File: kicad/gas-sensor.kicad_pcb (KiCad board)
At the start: 2 copper layers, 25 parts, among them J1 RJ12, U1 DS18B20, U2 FT232RL, U3 MCP1703A-3302_SOT23, U4 ATmega328P-AU, Y1 8MHz

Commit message: minor changes
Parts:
- added U5: DHT22, gas_sensor:DHT22, F.Cu at (60.9, 54.8)
- moved C3 96.5 mm to (76.9, 80.2), turned to 180 degrees
- moved C4 96.5 mm to (78.0, 85.4), turned to 180 degrees
- moved R2 83.9 mm to (84.5, 85.5)
- moved R1 63.9 mm to (105.1, 79.3), turned to 180 degrees
- moved R3 61.5 mm to (126.0, 72.2), turned to 180 degrees
- moved R4 53.8 mm to (143.1, 72.9), turned to 180 degrees
- moved C2 52.8 mm to (105.1, 82.8), turned to 180 degrees
- moved C6 33.7 mm to (125.8, 108.5)
- moved C5 33.6 mm to (125.3, 103.6), turned to 180 degrees
- moved C7 31.2 mm to (125.8, 110.8)
- moved U4 12.9 mm to (97.3, 97.8)
- moved D3 9.96 mm to (132.9, 105.8)
- moved U2 9.29 mm to (118.0, 93.2)
- moved D1 7.46 mm to (132.8, 96.4)
- moved U3 6.54 mm to (120.7, 106.4)
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
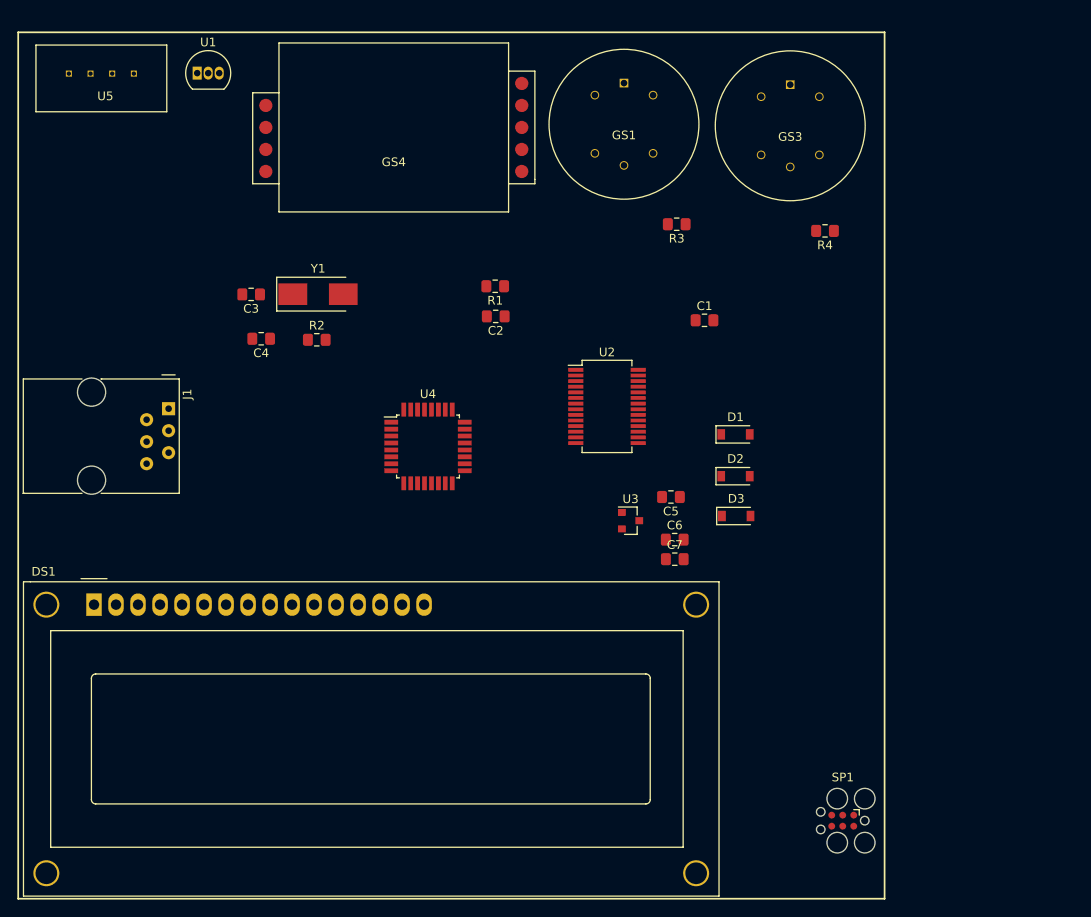
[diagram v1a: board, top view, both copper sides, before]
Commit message: First version of PCB
with 3D components
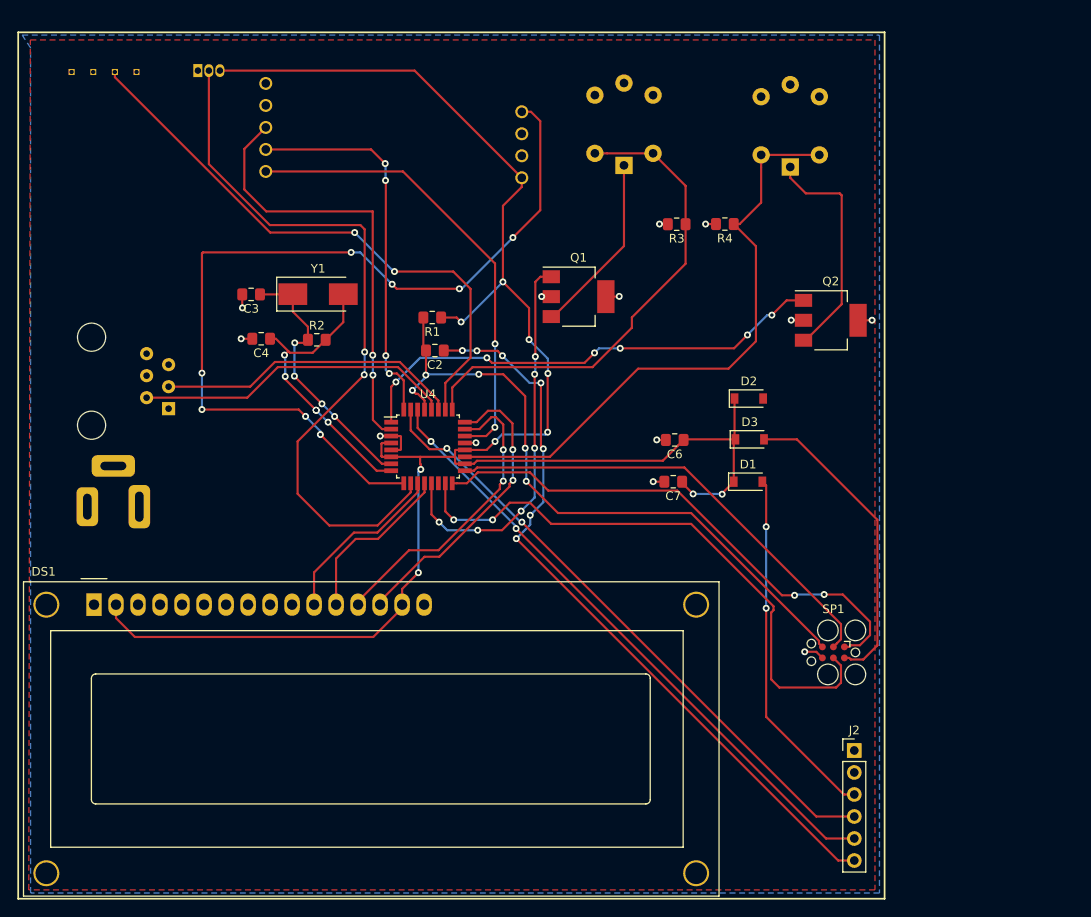
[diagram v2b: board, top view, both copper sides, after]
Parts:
- removed C1: 100nF, Capacitor_SMD:C_0805_2012Metric_Pad1.15x1.40mm_HandSolder
- removed C5: 10u, Capacitor_SMD:C_0805_2012Metric_Pad1.15x1.40mm_HandSolder
- removed U2: FT232RL, Package_SO:SSOP-28_5.3x10.2mm_P0.65mm
- removed U3: MCP1703A-3302_SOT23, Package_TO_SOT_SMD:SOT-23
- added J2: Conn FT232RL, Connector_PinHeader_2.54mm:PinHeader_1x06_P2.54mm_Vertical, F.Cu at (146.5, 132.9)
- added J3: PJ-017DH, gas_sensor:PC-017C, B.Cu at (58.0, 104.8)
- added Q1: BSP75, Package_TO_SOT_SMD:SOT-223-3_TabPin2, F.Cu at (114.7, 80.5)
- added Q2: BSP75, Package_TO_SOT_SMD:SOT-223-3_TabPin2, F.Cu at (143.8, 83.2)
- GS1, GS3, GS4, J1, U1, U5: moved to B.Cu
- moved SP1 19.5 mm to (144.1, 121.6)
- moved R4 11.6 mm to (131.6, 72.1)
- moved C6 11.5 mm to (125.8, 97.0), turned to 180 degrees
- moved D2 9.09 mm to (134.3, 92.3)
- moved D3 8.99 mm to (134.4, 97.0)
- moved C7 8.94 mm to (125.6, 101.9), turned to 180 degrees
- moved R1 8.11 mm to (97.8, 82.9)
- moved C2 8.05 mm to (98.1, 86.7)
- moved D1 5.65 mm to (134.2, 101.9)
- moved U5 2.20 mm to (58.7, 54.6), turned to 180 degrees
- moved U1 0.30 mm to (70.7, 54.4)
- turned GS4 to 180 degrees
- turned J1 to 90 degrees
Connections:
- net +BATT renamed Net-(J1-Pad5)
- C6 pad 1: +3V3 -> VCC
- C7 pad 1: +3V3 -> VCC
- D1 pad 1: Net-(C5-Pad1) -> VCC
- D2 pad 1: Net-(C5-Pad1) -> VCC
- D3 pad 1: Net-(C5-Pad1) -> VCC
- DS1 pad 15: +5V -> VCC
- DS1 pad 2: +5V -> VCC
- GS1 pad 1: +5V -> /Sensor1
- GS1 pad 2: +5V -> /Sensor1
- GS1 pad 3: /Sensor1 -> +5V
- GS1 pad 4: /Sensor1 -> +5V
- GS1 pad 6: GND -> Net-(GS1-Pad6)
- GS3 pad 1: +5V -> /Sensor2
- GS3 pad 2: +5V -> /Sensor2
- GS3 pad 3: /Sensor3 -> +5V
- GS3 pad 4: /Sensor3 -> +5V
- GS3 pad 6: GND -> Net-(GS3-Pad6)
- GS4 pad 1: /Sensor4 -> /Sensor3
- GS4 pad 6: +5V -> VCC
- J1 pad 1: +5V -> Net-(J1-Pad1)
- R1 pad 1: +3V3 -> VCC
- R4 pad 1: /Sensor3 -> /Sensor2
- U1 pad 3: +5V -> VCC
- U4 pad 1: Net-(U4-Pad1) -> /Sensor2_ON
- U4 pad 13: Net-(U4-Pad13) -> /Sensor1_ON
- U4 pad 19: /Sensor3 -> /Sensor2
- U4 pad 20: +5V -> VCC
- U4 pad 22: /Sensor4 -> /Sensor3
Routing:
- net VCC: track 0.00 -> 211.7 mm, vias 0 -> 10
- net /PWM_MH-Z19: track 0.00 -> 102.5 mm, vias 0 -> 8
- net /DTR: track 0.00 -> 86.5 mm, vias 0 -> 7
- net /TEMP: track 0.00 -> 82.8 mm, vias 0 -> 2
- net /RESET: track 0.00 -> 77.2 mm, vias 0 -> 5
- net /RX: track 0.00 -> 72.3 mm, vias 0 -> 2
- net /TX: track 0.00 -> 72.1 mm, vias 0 -> 2
- net /Sensor2: track 0.00 -> 70.1 mm
- net /MOSI: track 0.00 -> 67.8 mm, vias 0 -> 2
- net /HUM: track 0.00 -> 66.9 mm, vias 0 -> 2
- net /MISO: track 0.00 -> 61.0 mm, vias 0 -> 2
- net /Sensor1: track 0.00 -> 57.1 mm
- net /Sensor2_ON: track 0.00 -> 56.3 mm, vias 0 -> 6
- net /SCK: track 0.00 -> 54.1 mm
- net /Sensor3: track 0.00 -> 53.7 mm, vias 0 -> 2
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- added copper zone on F.Cu, net +5V
- added copper zone on B.Cu, net GND

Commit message: update
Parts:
- added C1: 100nF, Capacitor_SMD:C_0805_2012Metric_Pad1.15x1.40mm_HandSolder, F.Cu at (89.4, 88.0)
- added J4: hole, MountingHole:MountingHole_3.2mm_M3, F.Cu at (146.6, 53.5)
- added J5: hole, MountingHole:MountingHole_3.2mm_M3, F.Cu at (53.4, 139.3)
- added J6: hole, MountingHole:MountingHole_3.2mm_M3, F.Cu at (53.6, 53.6)
- added J7: hole, MountingHole:MountingHole_3.2mm_M3, F.Cu at (146.2, 138.8)
- added R5: R, Capacitor_SMD:C_0805_2012Metric_Pad1.15x1.40mm_HandSolder, F.Cu at (102.1, 102.7)
- J3: value PJ-017DH -> 5V_Power_source; footprint gas_sensor:PC-017C -> Connector_BarrelJack:BarrelJack_Horizontal
- Y1: footprint Crystal:Crystal_SMD_0603-2Pin_6.0x3.5mm_HandSoldering -> Crystal:Crystal_SMD_5032-2Pin_5.0x3.2mm_HandSoldering
- moved J2 100.1 mm to (53.9, 94.8)
- moved J3 80.3 mm to (136.1, 86.0), turned to 180 degrees
- moved SP1 17.2 mm to (145.0, 104.4)
- moved C3 16.6 mm to (81.0, 96.3), turned to 90 degrees
- moved Y1 13.5 mm to (86.0, 93.6), turned to 90 degrees
- moved Q2 12.3 mm to (135.6, 74.1), turned to 270 degrees
- moved DS1 11.0 mm to (66.5, 108.2)
- moved U5 10.0 mm to (60.6, 64.4), turned to 0 degrees
- moved R2 9.28 mm to (89.5, 93.3), turned to 90 degrees
- moved U1 9.26 mm to (61.5, 53.7)
- moved D1 9.06 mm to (127.7, 95.5)
- moved D3 8.94 mm to (127.7, 91.1)
- moved C2 8.87 mm to (93.5, 79.1), turned to 0 degrees
- moved D2 8.81 mm to (128.0, 86.1)
- moved J1 8.73 mm to (67.8, 84.7)
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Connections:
- DS1 pad 15: VCC -> Net-(DS1-Pad15)
- DS1 pad 3: Net-(DS1-Pad3) -> VCC
- DS1 pad 4: Net-(DS1-Pad4) -> /LCD_RS
- DS1 pad 5: Net-(DS1-Pad5) -> /LCD_RW
- DS1 pad 6: Net-(DS1-Pad6) -> /LCD_E
- J3 pad 3: GND -> (no net)
- U1 pad 3: VCC -> +5V
- U4 pad 15: /MOSI -> /LCD_E
- U4 pad 16: /MISO -> /LCD_RW
- U4 pad 17: /SCK -> /LCD_RS
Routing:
- net VCC: track 211.7 -> 0.00 mm, vias 10 -> 0
- net /PWM_MH-Z19: track 102.5 -> 0.00 mm, vias 8 -> 0
- net /DTR: track 86.5 -> 0.00 mm, vias 7 -> 0
- net /TEMP: track 82.8 -> 0.00 mm, vias 2 -> 0
- net /RESET: track 77.2 -> 0.00 mm, vias 5 -> 0
- net /RX: track 72.3 -> 0.00 mm, vias 2 -> 0
- net /TX: track 72.1 -> 0.00 mm, vias 2 -> 0
- net /Sensor2: track 70.1 -> 0.00 mm
- net /MOSI: track 67.8 -> 0.00 mm, vias 2 -> 0
- net /HUM: track 66.9 -> 0.00 mm, vias 2 -> 0
- net /MISO: track 61.0 -> 0.00 mm, vias 2 -> 0
- net /Sensor1: track 57.1 -> 0.00 mm
- net /Sensor2_ON: track 56.3 -> 0.00 mm, vias 6 -> 0
- net /SCK: track 54.1 -> 0.00 mm
- net /Sensor3: track 53.7 -> 0.00 mm, vias 2 -> 0
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- removed copper zone on F.Cu, net +5V
- removed copper zone on B.Cu, net GND

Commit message: Update
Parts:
- removed C7: 100nF, Capacitor_SMD:C_0805_2012Metric_Pad1.15x1.40mm_HandSolder
- removed GS4: MH-Z19, gas_sensor:MH-Z19
- removed U4: ATmega328P-AU, Package_QFP:TQFP-32_7x7mm_P0.8mm
- removed U5: DHT22, gas_sensor:DHT22
- added C5: 100nF, Capacitor_SMD:C_0805_2012Metric_Pad1.15x1.40mm_HandSolder, F.Cu at (84.2, 96.3)
- added GS2: MQ-8, gas_sensor:MQ-8, B.Cu at (112.9, 68.8)
- added U2: ATmega328P-AU, Package_QFP:TQFP-32_7x7mm_P0.8mm, F.Cu at (91.2, 97.3)
- added U3: DHT22, gas_sensor:DHT22, B.Cu at (60.0, 73.8)
- C1, C2: value 100nF -> 18pF
- C3: value 18pF -> 10u
- C4: value 18pF -> 100nF
- C6: value 10u -> 100nF
- GS3: value MQ-8 -> MH-Z19; footprint gas_sensor:MQ-8 -> gas_sensor:MH-Z19
- J1: value RJ12 -> Conn FT232RL; footprint Connector_RJ:RJ12_Amphenol_54601 -> Connector_PinHeader_2.54mm:PinHeader_1x06_P2.54mm_Vertical
- J2: value Conn FT232RL -> RJ12; footprint Connector_PinHeader_2.54mm:PinHeader_1x06_P2.54mm_Vertical -> Connector_RJ:RJ12_Amphenol_54601; moved to B.Cu
- J3: value 5V_Power_source -> hole; footprint Connector_BarrelJack:BarrelJack_Horizontal -> MountingHole:MountingHole_3.2mm_M3
- J7: value hole -> 5V_Power_source; footprint MountingHole:MountingHole_3.2mm_M3 -> Connector_BarrelJack:BarrelJack_Horizontal; moved to B.Cu
- R1: value 10k -> 1M
- R2: value 1M -> R
- R3: value 20k -> 10k
- R4: value 10k -> 20k
- R5: value R -> 10k; footprint Capacitor_SMD:C_0805_2012Metric_Pad1.15x1.40mm_HandSolder -> Resistor_SMD:R_0805_2012Metric_Pad1.15x1.40mm_HandSolder
- moved J1 86.8 mm to (142.8, 128.4), turned to 0 degrees
- moved J3 60.2 mm to (146.0, 145.4)
- moved GS3 51.6 mm to (84.8, 69.7)
- moved J7 47.4 mm to (130.8, 94.0), turned to 180 degrees
- moved R3 33.8 mm to (92.8, 88.5)
- moved C3 33.7 mm to (114.5, 100.5), turned to 270 degrees
- moved C6 31.6 mm to (90.6, 88.4), turned to 270 degrees
- moved C2 30.9 mm to (76.9, 105.2), turned to 180 degrees
- moved C4 30.7 mm to (110.8, 100.5)
- moved Q2 29.2 mm to (107.7, 82.5), turned to 180 degrees
- moved R1 26.4 mm to (84.5, 101.9), turned to 270 degrees
- moved R5 23.8 mm to (115.0, 82.6), turned to 180 degrees
- moved R2 20.7 mm to (103.8, 108.3), turned to 270 degrees
- moved GS1 20.6 mm to (133.3, 68.7)
- moved C1 17.4 mm to (77.0, 100.2), turned to 180 degrees
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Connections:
- C1 pad 1: VCC -> /XTAL1
- C2 pad 1: /DTR -> /XTAL2
- C2 pad 2: /RESET -> GND
- C3 pad 1: /XTAL1 -> VCC
- C4 pad 1: /XTAL2 -> VCC
- C6 pad 1: VCC -> /DTR
- C6 pad 2: GND -> /RESET
- DS1 pad 12: /LCD2 -> /LCD2_MOSI
- DS1 pad 13: /LCD3 -> /LCD3_MISO
- DS1 pad 14: /LCD4 -> /LCD4_SCK
- GS3 pad 1: /Sensor2 -> /Sensor3
- GS3 pad 2: /Sensor2 -> /RX_MH-Z19
- GS3 pad 3: +5V -> /TX_MH-Z19
- GS3 pad 4: +5V -> Net-(GS3-Pad4)
- GS3 pad 5: +5V -> Net-(GS3-Pad5)
- GS3 pad 6: Net-(GS3-Pad6) -> VCC
- J1 pad 1: Net-(J1-Pad1) -> GND
- J1 pad 2: /SCL -> Net-(J1-Pad2)
- J1 pad 3: /SDA -> /VCC-FTDI
- J1 pad 4: GND -> /TX
- J1 pad 5: Net-(J1-Pad5) -> /RX
- J1 pad 6: GND -> /DTR
- J2 pad 1: GND -> Net-(J2-Pad1)
- J2 pad 2: Net-(J2-Pad2) -> /SCL
- J2 pad 3: /VCC-FTDI -> /SDA
- J2 pad 4: /TX -> GND
- J2 pad 5: /RX -> Net-(J2-Pad5)
- J2 pad 6: /DTR -> GND
- J3 pad 1: +5V -> Net-(J3-Pad1)
- J7 pad 1: Net-(J7-Pad1) -> +5V
- Q2 pad 3: Net-(GS3-Pad6) -> Net-(GS2-Pad6)
- R1 pad 1: VCC -> /XTAL1
- R1 pad 2: /RESET -> /XTAL2
- R2 pad 1: /XTAL1 -> /LCD_LED
- R2 pad 2: /XTAL2 -> Net-(DS1-Pad15)
- R3 pad 1: /Sensor1 -> VCC
- R3 pad 2: GND -> /RESET
- R4 pad 1: /Sensor2 -> /Sensor1
- R5 pad 1: /LCD_LED -> /Sensor2
- R5 pad 2: Net-(DS1-Pad15) -> GND
- SP1 pad 1: /MISO -> /LCD3_MISO
- SP1 pad 3: /SCK -> /LCD4_SCK
- SP1 pad 4: /MOSI -> /LCD2_MOSI
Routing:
- net VCC: track 0.00 -> 185.3 mm
- net GND: track 0.00 -> 101.9 mm, vias 0 -> 17
- net /LCD4_SCK: track 0.00 -> 88.8 mm, vias 0 -> 4
- net /DTR: track 0.00 -> 81.0 mm, vias 0 -> 2
- net /LCD3_MISO: track 0.00 -> 77.5 mm, vias 0 -> 6
- net /LCD2_MOSI: track 0.00 -> 72.5 mm, vias 0 -> 6
- net /TX: track 0.00 -> 69.7 mm, vias 0 -> 4
- net /RX: track 0.00 -> 66.6 mm, vias 0 -> 4
- net /Sensor1: track 0.00 -> 64.9 mm
- net /RESET: track 0.00 -> 64.6 mm, vias 0 -> 4
- net /TEMP: track 0.00 -> 50.4 mm, vias 0 -> 2
- net /Sensor2: track 0.00 -> 44.0 mm
- net /Sensor1_ON: track 0.00 -> 40.8 mm
- net /HUM: track 0.00 -> 39.5 mm, vias 0 -> 2
- net /Sensor3: track 0.00 -> 33.0 mm, vias 0 -> 2
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- added copper zone on F.Cu, net +5V
- added copper zone on B.Cu, net GND

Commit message: Update
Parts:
- added J10: hole, MountingHole:MountingHole_3.2mm_M3, F.Cu at (53.8, 76.2)
- added J11: hole, MountingHole:MountingHole_3.2mm_M3, F.Cu at (53.8, 83.8)
- added J8: hole, MountingHole:MountingHole_3.2mm_M3, F.Cu at (146.2, 76.2)
- added J9: hole, MountingHole:MountingHole_3.2mm_M3, F.Cu at (146.2, 83.8)
- moved J4 10.2 mm to (146.2, 53.8)
- moved J6 10.2 mm to (53.8, 53.8)
- moved U1 7.46 mm to (65.0, 57.5), turned to 180 degrees
- moved GS1 6.18 mm to (134.3, 62.6)
- moved R4 6.18 mm to (136.1, 75.3)
- moved R5 6.18 mm to (115.9, 76.5)
- moved U3 6.18 mm to (60.9, 67.7)
- moved GS2 6.18 mm to (113.9, 62.7)
- moved GS3 6.18 mm to (85.8, 63.6)
- moved J7 5.52 mm to (136.1, 92.4)
- moved Q2 1.24 mm to (107.7, 81.3)
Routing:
- net GND: track 101.9 -> 131.4 mm, vias 17 -> 16
- net +5V: track 9.57 -> 0.33 mm, vias 1 -> 0
- net /Sensor1: track 64.9 -> 71.5 mm
- net /RX_MH-Z19: track 28.5 -> 35.0 mm
- net /TX_MH-Z19: track 26.6 -> 33.1 mm
- net /Sensor3: track 33.0 -> 39.5 mm
- net /Sensor2: track 44.0 -> 50.5 mm
- net Net-(GS1-Pad6): track 6.65 -> 13.0 mm
- net VCC: track 185.3 -> 191.4 mm
- net /TEMP: track 50.4 -> 56.2 mm
- net /HUM: track 39.5 -> 45.3 mm
- net /PWM_MH-Z19: track 30.0 -> 35.7 mm
- net Net-(GS2-Pad6): track 7.75 -> 12.9 mm
- net /RESET: track 64.6 -> 61.2 mm
- net /DTR: track 81.0 -> 79.3 mm
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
